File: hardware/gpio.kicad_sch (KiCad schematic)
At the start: 3 parts, among them U2 W65C22SxP, U4 W65C22SxP, U5 74AHC1G04

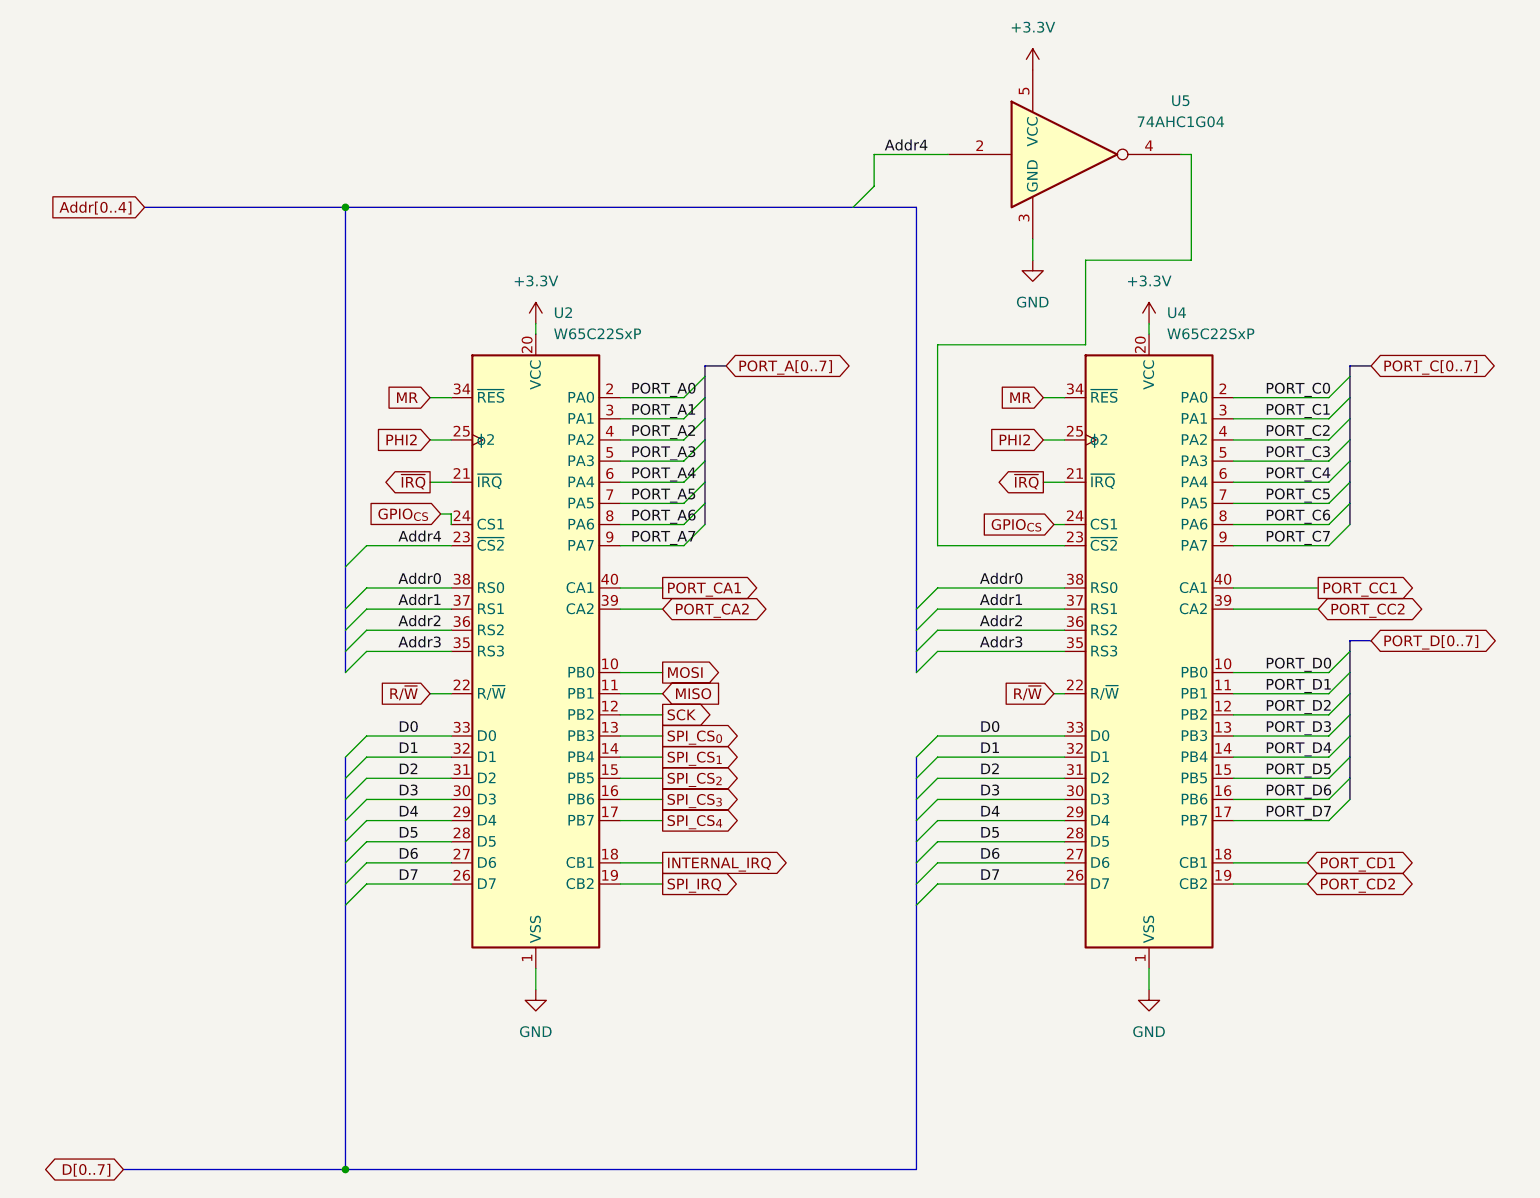
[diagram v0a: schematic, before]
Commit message: Changed Ethernet Chip to Ethernet ModuleWIZ850IO
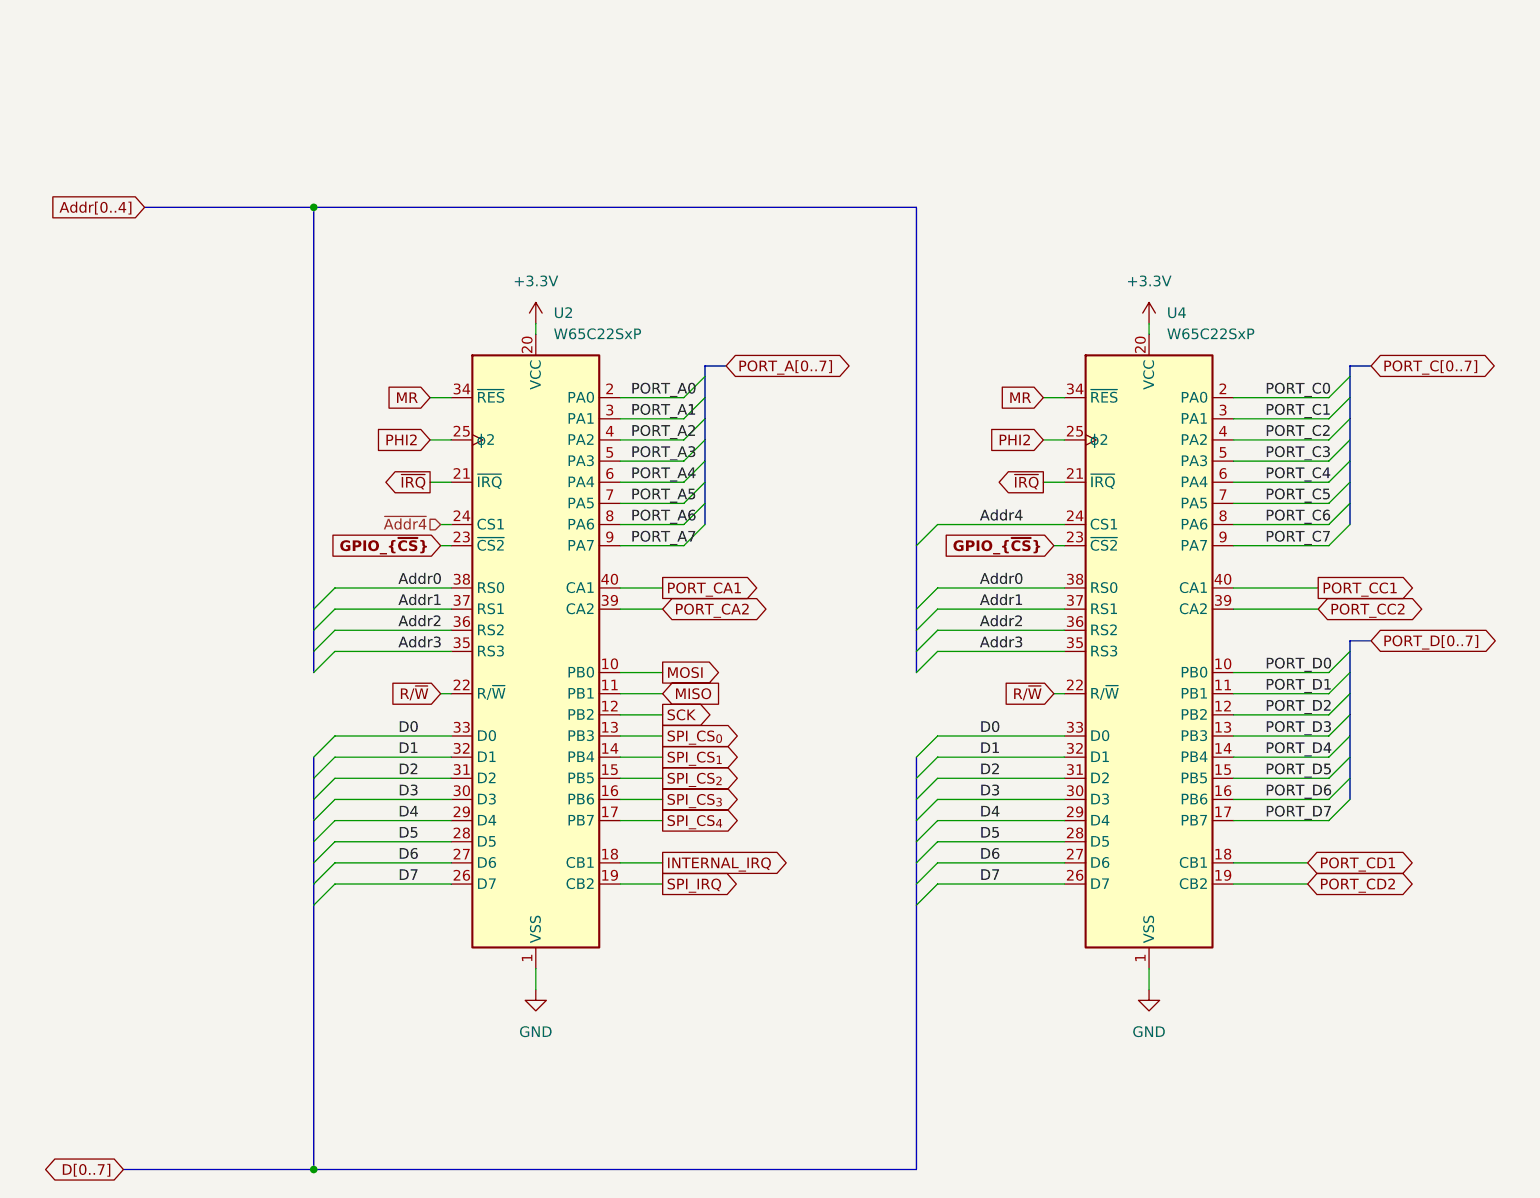
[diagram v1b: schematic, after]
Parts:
- removed U5: 74AHC1G04, Package_TO_SOT_SMD:SOT-23-5, symbol 74xGxx:74AHC1G04
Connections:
- net Addr4: now also U4.24 (CS1); no longer U2.23 (~{CS2})
- net GPIO_{~{CS}}: now reaches U4.23 (~{CS2})
- net GPIO_{~{CS}}: now also U2.23 (~{CS2})
- net GPIO_{CS} renamed ~{Addr4}
- net ~{Addr4}: no longer U4.24 (CS1)

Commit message: Fixes and addres fix adding VDA AND VPA
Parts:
- added R1, R2: 10k, Resistor_SMD:R_0603_1608Metric, symbol Device:R_Small_US
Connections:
- net +3.3V: now also R1.1, R2.1
- net INTERNAL_IRQ: now also R2.2
- net SPI_IRQ: now also R1.2
- net PHI2 renamed CLK

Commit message: PCD DESIGN
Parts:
- renumbered U2 to VIA1, U4 to VIA2
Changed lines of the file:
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@@
 		(dnp no)
 		(fields_autoplaced yes)
-		(property "Reference" "U4"
+		(property "Reference" "VIA2"
 			(at 196.4533 57.15 0)
 			(effects
@@
 			(project "Lambda One"
 				(path "/73ea9964-373f-4fdc-b03e-f532cf836c0d/c99586b2-79bd-4011-9acf-fcc28a8dd9c0"
-					(reference "U4")
+					(reference "VIA2")
 					(unit 1)
 				)
@@
 		(dnp no)
 		(fields_autoplaced yes)
-		(property "Reference" "U2"
+		(property "Reference" "VIA1"
 			(at 122.7933 57.15 0)
 			(effects
@@
 			(project "Lambda One"
 				(path "/73ea9964-373f-4fdc-b03e-f532cf836c0d/c99586b2-79bd-4011-9acf-fcc28a8dd9c0"
-					(reference "U2")
+					(reference "VIA1")
 					(unit 1)
 				)

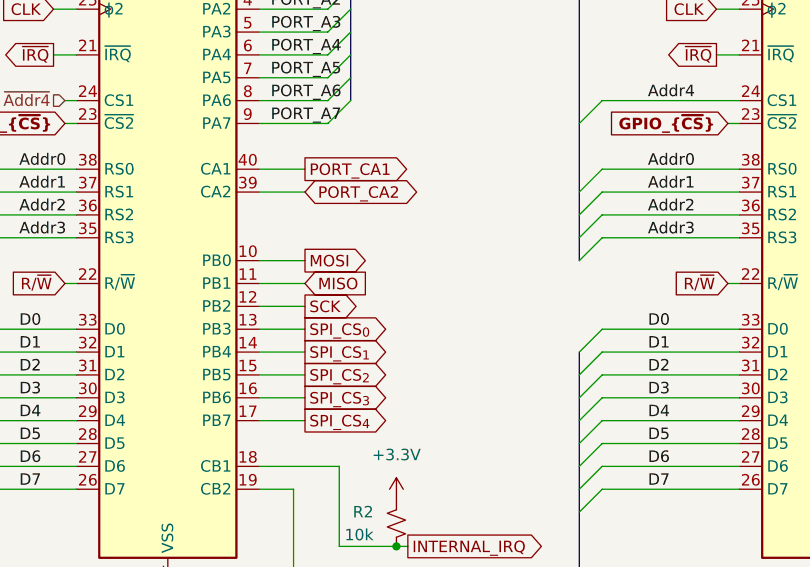
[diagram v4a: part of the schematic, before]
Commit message: Added 2.42 Inches OLED Display
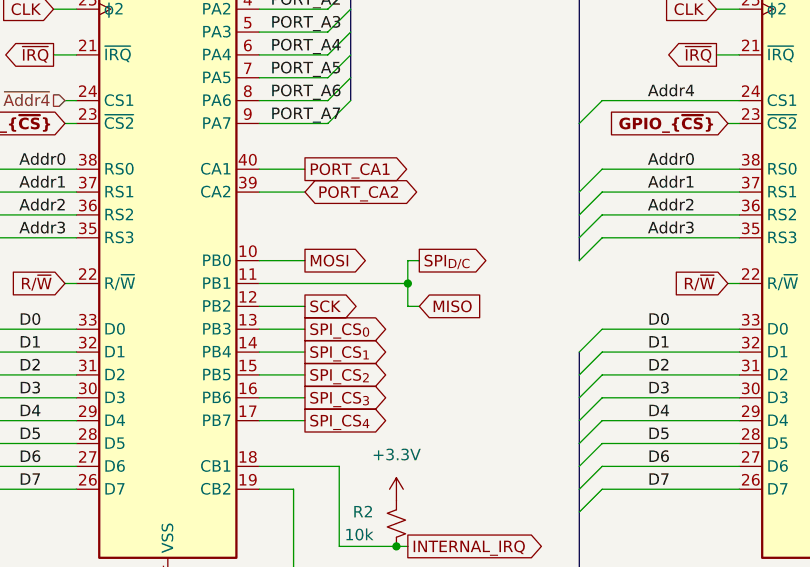
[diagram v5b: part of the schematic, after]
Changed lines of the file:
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@@
+		(color 0 0 0 0)
+	)
+	(junction
+		(at 147.32 102.87)
+		(diameter 0)
 		(color 0 0 0 0)
 	)
@@
 	(wire
 		(pts
-			(xy 130.81 102.87) (xy 135.89 102.87)
+			(xy 147.32 105.41) (xy 148.59 105.41)
+		)
+		(stroke
+			(width 0)
+			(type default)
+		)
+	)
+	(wire
+		(pts
+			(xy 130.81 102.87) (xy 147.32 102.87)
 		)
 		(stroke
@@
 	(wire
 		(pts
+			(xy 147.32 105.41) (xy 147.32 102.87)
+		)
+		(stroke
+			(width 0)
+			(type default)
+		)
+	)
+	(wire
+		(pts
 			(xy 130.81 82.55) (xy 138.43 82.55)
 		)
@@
 	(wire
 		(pts
+			(xy 147.32 100.33) (xy 147.32 102.87)
+		)
+		(stroke
+			(width 0)
+			(type default)
+		)
+	)
+	(wire
+		(pts
 			(xy 168.91 82.55) (xy 184.15 82.55)
 		)
@@
 		(pts
 			(xy 168.91 113.03) (xy 184.15 113.03)
+		)
+		(stroke
+			(width 0)
+			(type default)
+		)
+	)
+	(wire
+		(pts
+			(xy 148.59 100.33) (xy 147.32 100.33)
 		)
 		(stroke
@@
 	(global_label "MISO"
 		(shape input)
-		(at 135.89 102.87 0)
-		(fields_autoplaced yes)
+		(at 148.59 105.41 0)
 		(effects
 			(font
@@
 		)
 		(property "Intersheetrefs" "${INTERSHEET_REFS}"
-			(at 143.4714 102.87 0)
+			(at 156.1714 105.41 0)
 			(effects
 				(font
@@
 			(effects
 				(font
+					(size 1.27 1.27)
+				)
+				(justify left)
+				(hide yes)
+			)
+		)
+	)
+	(global_label "SPI_{D{slash}C}"
+		(shape output)
+		(at 148.59 100.33 0)
+		(fields_autoplaced yes)
+		(effects
+			(font
+				(size 1.27 1.27)
+			)
+			(justify left)
+		)
+		(property "Intersheetrefs" "${INTERSHEET_REFS}"
+			(at 157.8067 100.33 0)
+			(effects
+				(font

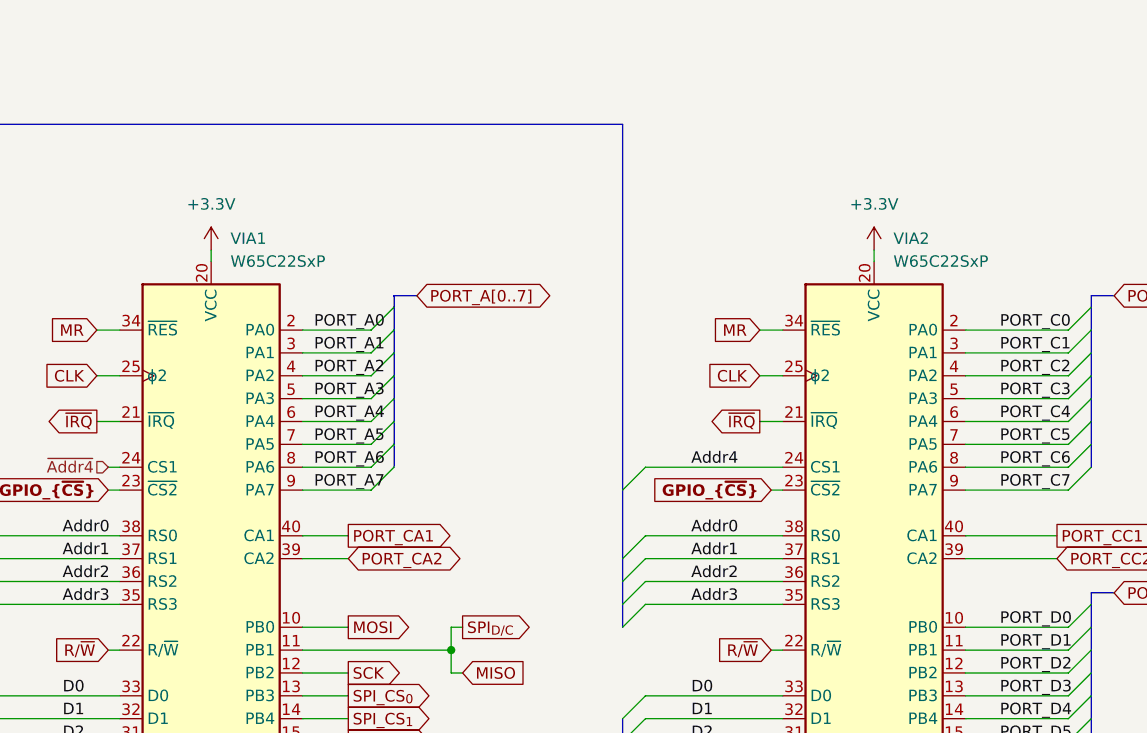
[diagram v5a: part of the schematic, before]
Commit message: Removed old VPU
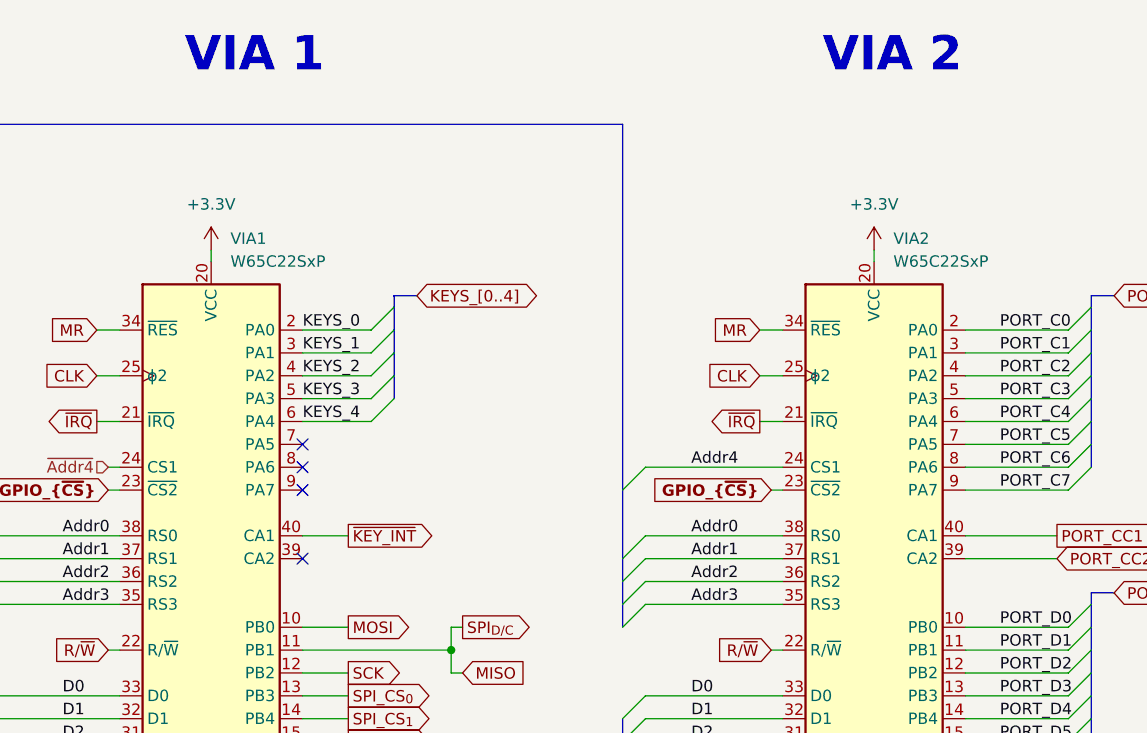
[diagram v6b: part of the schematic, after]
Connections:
- net PORT_A0 renamed KEYS_0
- net PORT_A1 renamed KEYS_1
- net PORT_A2 renamed KEYS_2
- net PORT_A3 renamed KEYS_3
- net PORT_A4 renamed KEYS_4
- net PORT_A5: no longer names the net of VIA1.7 (PA5)
- net PORT_A6: no longer names the net of VIA1.8 (PA6)
- net PORT_A7: no longer names the net of VIA1.9 (PA7)
- net PORT_CA1 renamed ~{KEY_INT}
- net PORT_CA2: no longer names the net of VIA1.39 (CA2)
- no-connect marks 0 -> 4
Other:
- note added: "VIA 1"
- note added: "VIA 2"
